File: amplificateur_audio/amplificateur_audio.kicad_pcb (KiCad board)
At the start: 2 copper layers, 54 parts, among them J2 Conn_01x02, J3 Conn_01x03, K1 Relay_1CT, Q1 Q_PNP_EBC, Q10 Q_PNP_BCE, Q11 BC636, Q12 Q_NPN_BCE, Q13 Q_NPN_EBC, Q2 Q_PNP_EBC, Q3 Q_PNP_EBC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

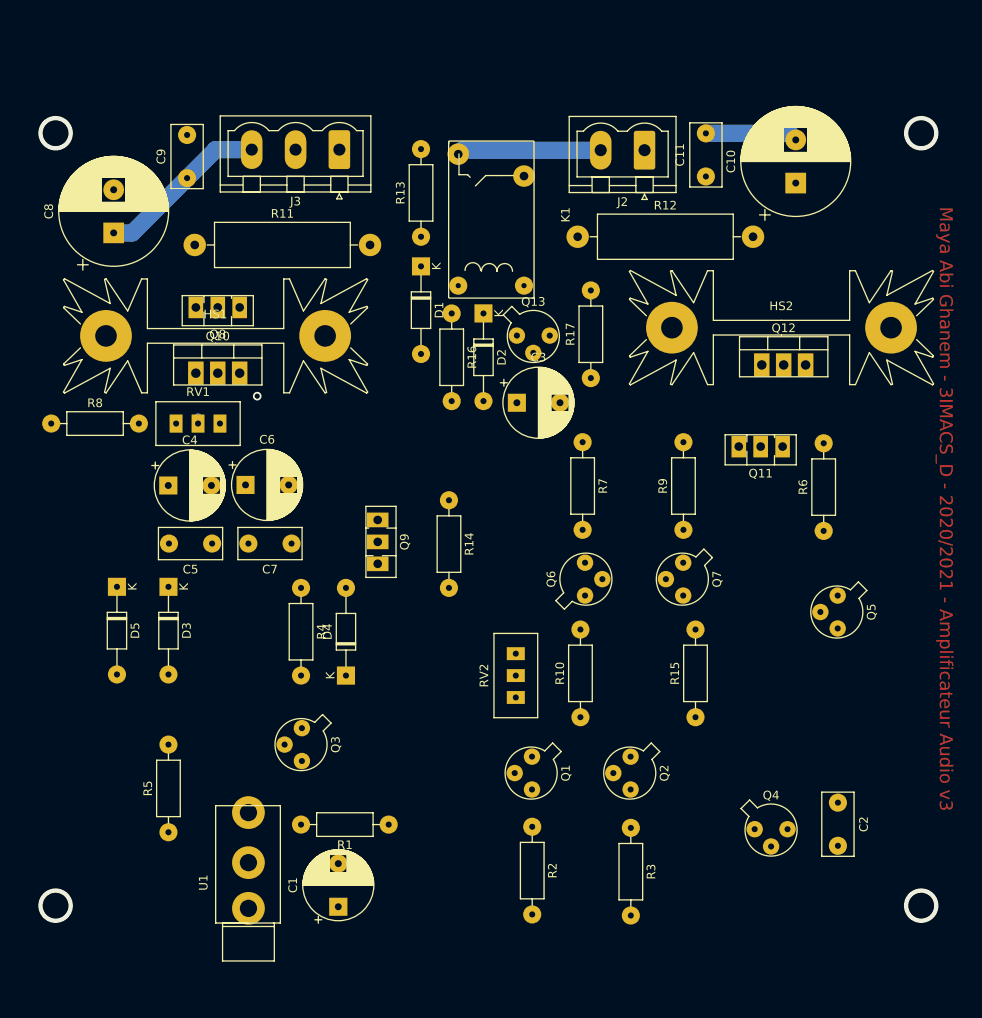
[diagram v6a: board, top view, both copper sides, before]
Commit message: pcb modifie sans vias
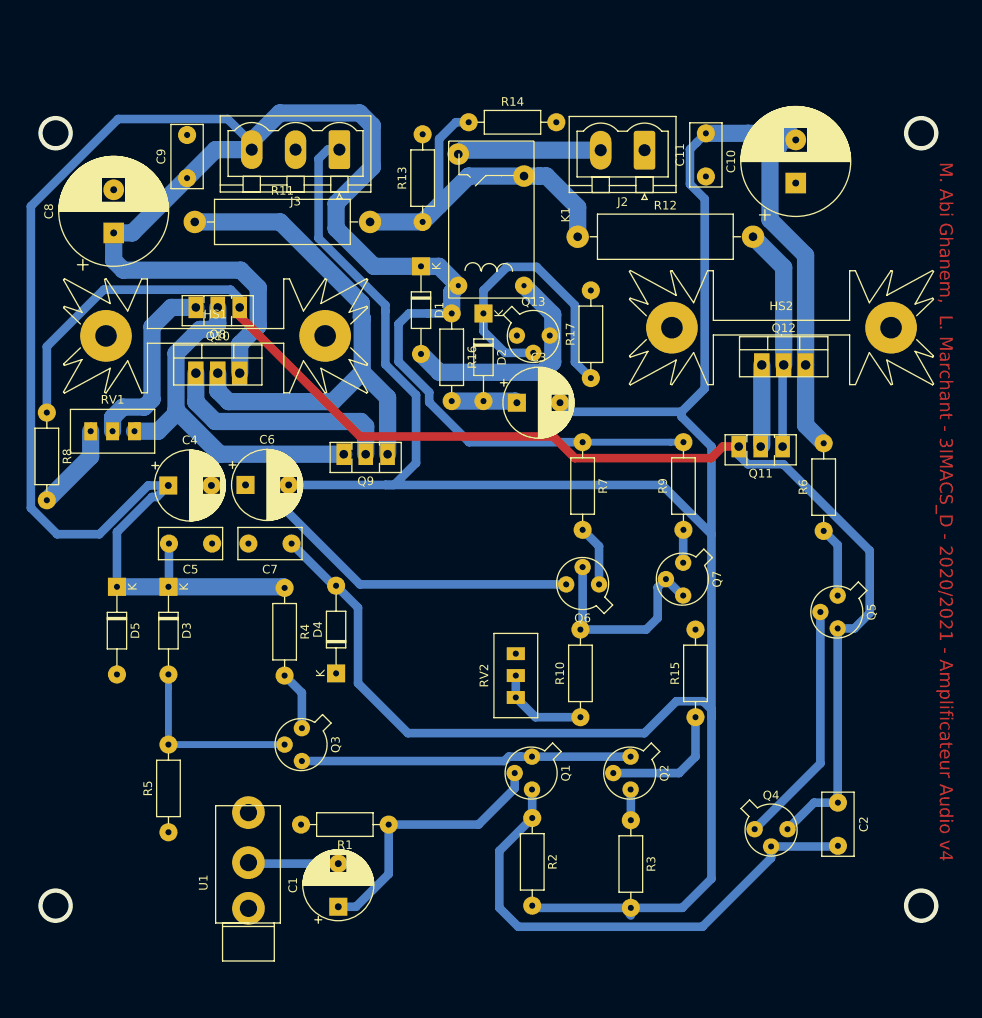
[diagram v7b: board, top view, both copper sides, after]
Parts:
- moved R14 43.9 mm to (84.7, 45.7), turned to 0 degrees
- moved RV1 9.95 mm to (46.0, 81.5)
- moved Q9 7.71 mm to (75.3, 84.2), turned to 180 degrees
- moved R11 2.67 mm to (53.0, 57.3)
- moved R4 1.91 mm to (63.4, 99.7)
- moved R13 1.73 mm to (79.4, 57.3)
- moved R8 1.37 mm to (35.8, 79.4), turned to 270 degrees
- moved D4 1.17 mm to (69.3, 109.6)
- moved Q6 1.17 mm to (99.2, 99.2), turned to 180 degrees
- moved R2 1.02 mm to (92.1, 126.4)
- moved R3 0.89 mm to (103.5, 126.6)
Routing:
- net -12V: track 12.4 -> 353.8 mm
- net +12V: track 20.0 -> 276.9 mm
- net Net-(C2-Pad1): track 0.04 -> 160.2 mm
- net Net-(Q6-Pad3): track 0.18 -> 91.7 mm
- net Net-(Q10-Pad2): track 0.76 -> 62.7 mm, vias 1 -> 0
- net Net-(C2-Pad2): track 0.11 -> 60.1 mm
- net Net-(K1-Padc1): track 0.00 -> 43.1 mm
- net Net-(Q1-Pad1): track 0.00 -> 38.3 mm
- net Net-(D2-Pad1): track 0.00 -> 34.3 mm
- net Net-(C1-Pad1): track 0.00 -> 31.3 mm
- net Net-(Q4-Pad1): track 0.00 -> 28.3 mm
- net Net-(Q10-Pad1): track 0.00 -> 27.4 mm
- net Net-(D1-Pad2): track 0.00 -> 26.9 mm
- net Net-(Q11-Pad1): track 0.97 -> 26.8 mm
- net Net-(Q6-Pad2): track 0.10 -> 24.5 mm
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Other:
- board text added: "M. Abi Ghanem, L. Marchant - 3IMACS_D - 2020/2021 - Amplificateur Audio v4"
- board text removed: "Maya Abi Ghanem - 3IMACS_D - 2020/2021 - Amplificateur Audio v3"

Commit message: ajout de plan de masse couche front
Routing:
- added copper zone on F.Cu, net GND
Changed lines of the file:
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@@
   (segment (start 49.911 109.728) (end 49.911 111.212924) (width 0.8) (layer B.Cu) (net 31))
   (segment (start 63.373 117.856) (end 49.911 117.856) (width 0.8) (layer B.Cu) (net 31))
+  (zone (net 7) (net_name GND) (layer F.Cu) (hatch edge 0.508)
+    (connect_pads (clearance 0.508))
+    (min_thickness 0.254)
+    (fill yes (arc_segments 16) (thermal_gap 0.508) (thermal_bridge_width 0.508))
+    (polygon
+      (pts
+        (xy 142.24 43.18) (xy 142.24 139.7) (xy 32.385 139.7) (xy 32.385 43.18)
+      )
+    )
+  )
 )
